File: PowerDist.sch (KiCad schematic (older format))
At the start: 13 parts, among them J7 PowerConn, U2 RI3-1205S, U3 NCP1117-3.3_SOT223

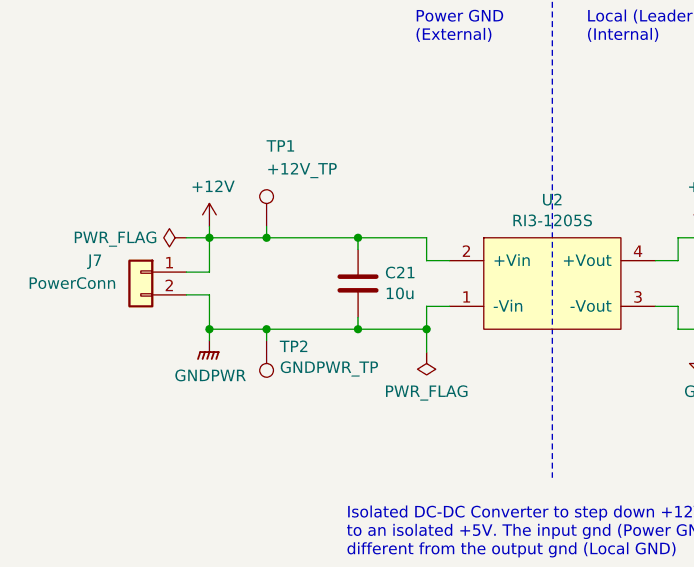
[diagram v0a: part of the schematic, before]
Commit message: adds necessary resistors, keep out zones, and TVS diode
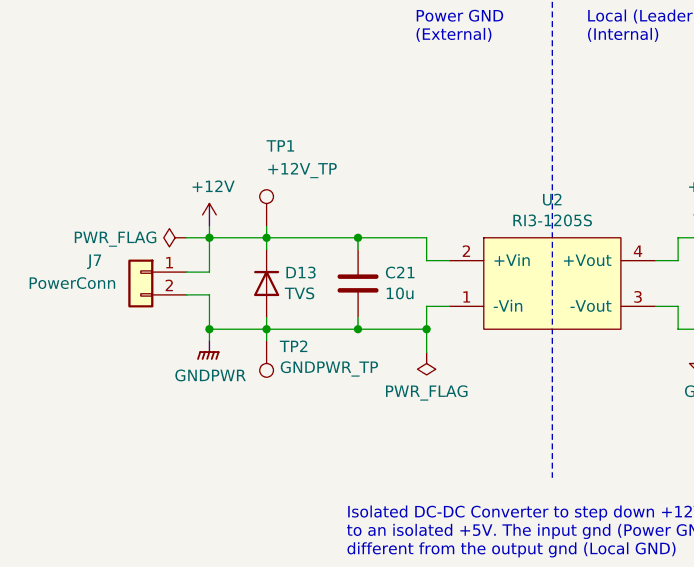
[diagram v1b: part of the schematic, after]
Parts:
- added D13: TVS, Diode_SMD:D_SOD-323, symbol Simulation_SPICE:DIODE
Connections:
- net +12V: now also D13.2 (K)
- net GNDPWR: now also D13.1 (A)
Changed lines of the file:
@@
 EESchema Schematic File Version 4
-LIBS:Telemetry-Primary-cache
-EELAYER 26 0
+EELAYER 30 0
 EELAYER END
 $Descr A4 11693 8268
@@
 Wire Wire Line
 	3950 3500 3950 3600
+$Comp
+L Simulation_SPICE:DIODE D13
+U 1 1 6163B945
+P 3250 3400
+F 0 "D13" V 3296 3320 50  0000 R CNN
+F 1 "TVS" V 3205 3320 50  0000 R CNN
+F 2 "Diode_SMD:D_SOD-323" H 3250 3400 50  0001 C CNN
+F 3 "~" H 3250 3400 50  0001 C CNN
+F 4 "Y" H 3250 3400 50  0001 L CNN "Spice_Netlist_Enabled"
+F 5 "D" H 3250 3400 50  0001 L CNN "Spice_Primitive"
+	1    3250 3400
+	0    -1   -1   0
+$EndComp
+Wire Wire Line
+	3250 3250 3250 3200
+Wire Wire Line
+	3250 3550 3250 3600
 $EndSCHEMATC
